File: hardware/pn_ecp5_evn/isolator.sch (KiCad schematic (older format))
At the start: 12 parts, among them U901 ADS7868, U902 ADS7868, U903 Si8640BB-B-IU, U904 Si8640BB-B-IU, U905 Si8642BB-B-IU

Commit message: first pass footprint assignment on pn r0
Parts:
- C901, C902: value C_Small -> 1 uF; footprint (none) -> Capacitor_SMD:C_0402_1005Metric
- C903, C904, C906, C907: value C_Small -> 100 nF; footprint (none) -> Capacitor_SMD:C_0402_1005Metric
- C905: value C_Small -> DNI; footprint (none) -> Capacitor_SMD:C_0402_1005Metric
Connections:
- net BUF_~PD: now reaches U905.11 (B4)
- net BUF_~PD~_ISO: now reaches U905.6 (A4)
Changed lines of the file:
@@
 P 2500 3950
 F 0 "C902" H 2592 3996 50  0000 L CNN
-F 1 "C_Small" H 2592 3905 50  0000 L CNN
-F 2 "" H 2500 3950 50  0001 C CNN
+F 1 "1 uF" H 2592 3905 50  0000 L CNN
+F 2 "Capacitor_SMD:C_0402_1005Metric" H 2500 3950 50  0001 C CNN
 F 3 "~" H 2500 3950 50  0001 C CNN
 	1    2500 3950
@@
 P 2500 2150
 F 0 "C901" H 2592 2196 50  0000 L CNN
-F 1 "C_Small" H 2592 2105 50  0000 L CNN
-F 2 "" H 2500 2150 50  0001 C CNN
+F 1 "1 uF" H 2592 2105 50  0000 L CNN
+F 2 "Capacitor_SMD:C_0402_1005Metric" H 2500 2150 50  0001 C CNN
 F 3 "~" H 2500 2150 50  0001 C CNN
 	1    2500 2150
@@
 P 5500 5850
 F 0 "C905" V 5271 5850 50  0000 C CNN
-F 1 "C_Small" V 5362 5850 50  0000 C CNN
-F 2 "" H 5500 5850 50  0001 C CNN
+F 1 "DNI" V 5362 5850 50  0000 C CNN
+F 2 "Capacitor_SMD:C_0402_1005Metric" H 5500 5850 50  0001 C CNN
 F 3 "~" H 5500 5850 50  0001 C CNN
 	1    5500 5850
@@
 P 7350 1850
 F 0 "C906" H 7442 1896 50  0000 L CNN
-F 1 "C_Small" H 7442 1805 50  0000 L CNN
-F 2 "" H 7350 1850 50  0001 C CNN
+F 1 "100 nF" H 7442 1805 50  0000 L CNN
+F 2 "Capacitor_SMD:C_0402_1005Metric" H 7350 1850 50  0001 C CNN
 F 3 "~" H 7350 1850 50  0001 C CNN
 	1    7350 1850
@@
 P 7900 1850
 F 0 "C907" H 7992 1896 50  0000 L CNN
-F 1 "C_Small" H 7992 1805 50  0000 L CNN
-F 2 "" H 7900 1850 50  0001 C CNN
+F 1 "100 nF" H 7992 1805 50  0000 L CNN
+F 2 "Capacitor_SMD:C_0402_1005Metric" H 7900 1850 50  0001 C CNN
 F 3 "~" H 7900 1850 50  0001 C CNN
 	1    7900 1850
@@
 P 3750 5900
 F 0 "C904" H 3842 5946 50  0000 L CNN
-F 1 "C_Small" H 3842 5855 50  0000 L CNN
-F 2 "" H 3750 5900 50  0001 C CNN
+F 1 "100 nF" H 3842 5855 50  0000 L CNN
+F 2 "Capacitor_SMD:C_0402_1005Metric" H 3750 5900 50  0001 C CNN
 F 3 "~" H 3750 5900 50  0001 C CNN
 	1    3750 5900
@@
 P 3150 5900
 F 0 "C903" H 3242 5946 50  0000 L CNN
-F 1 "C_Small" H 3242 5855 50  0000 L CNN
-F 2 "" H 3150 5900 50  0001 C CNN
+F 1 "100 nF" H 3242 5855 50  0000 L CNN
+F 2 "Capacitor_SMD:C_0402_1005Metric" H 3150 5900 50  0001 C CNN
 F 3 "~" H 3150 5900 50  0001 C CNN
 	1    3150 5900
@@
 Wire Wire Line
 	3150 5650 3150 5800
+Text HLabel 6400 5100 2    50   Input ~ 0
+BUF_~PD
+Wire Wire Line
+	6400 5100 5900 5100
+Text HLabel 4600 5100 0    50   Output ~ 0
+BUF_~PD~_ISO
+Wire Wire Line
+	4600 5100 5100 5100
 $EndSCHEMATC

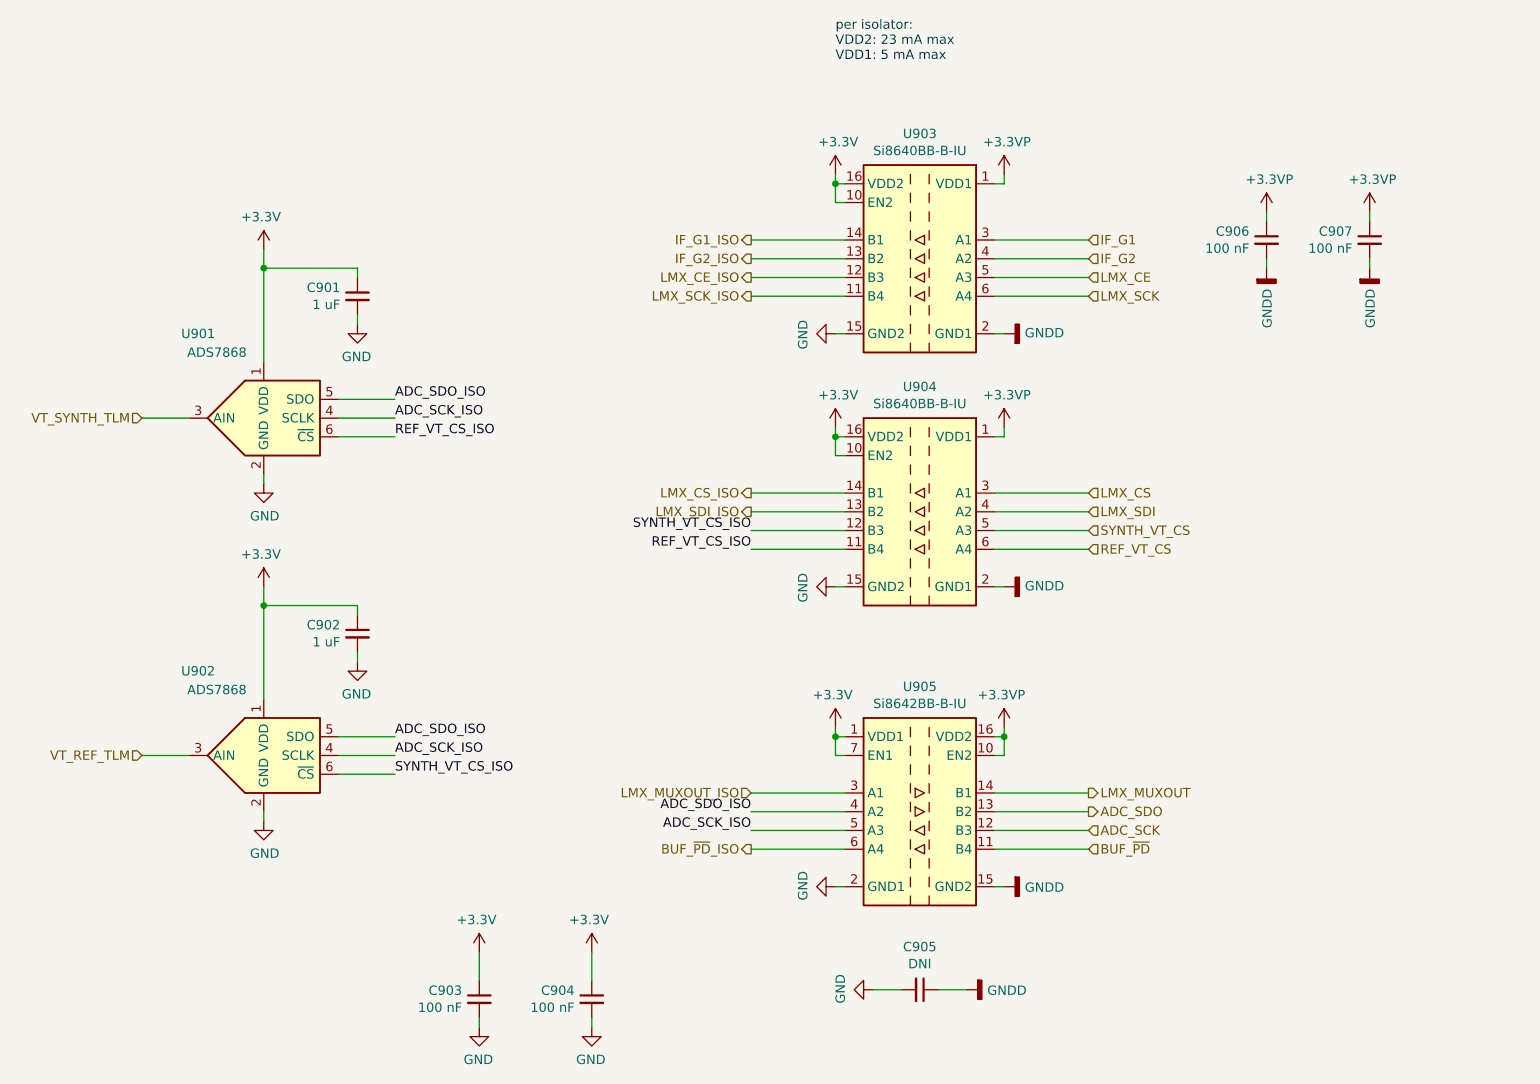
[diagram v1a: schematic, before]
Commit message: started component placement on phase noise analyzer
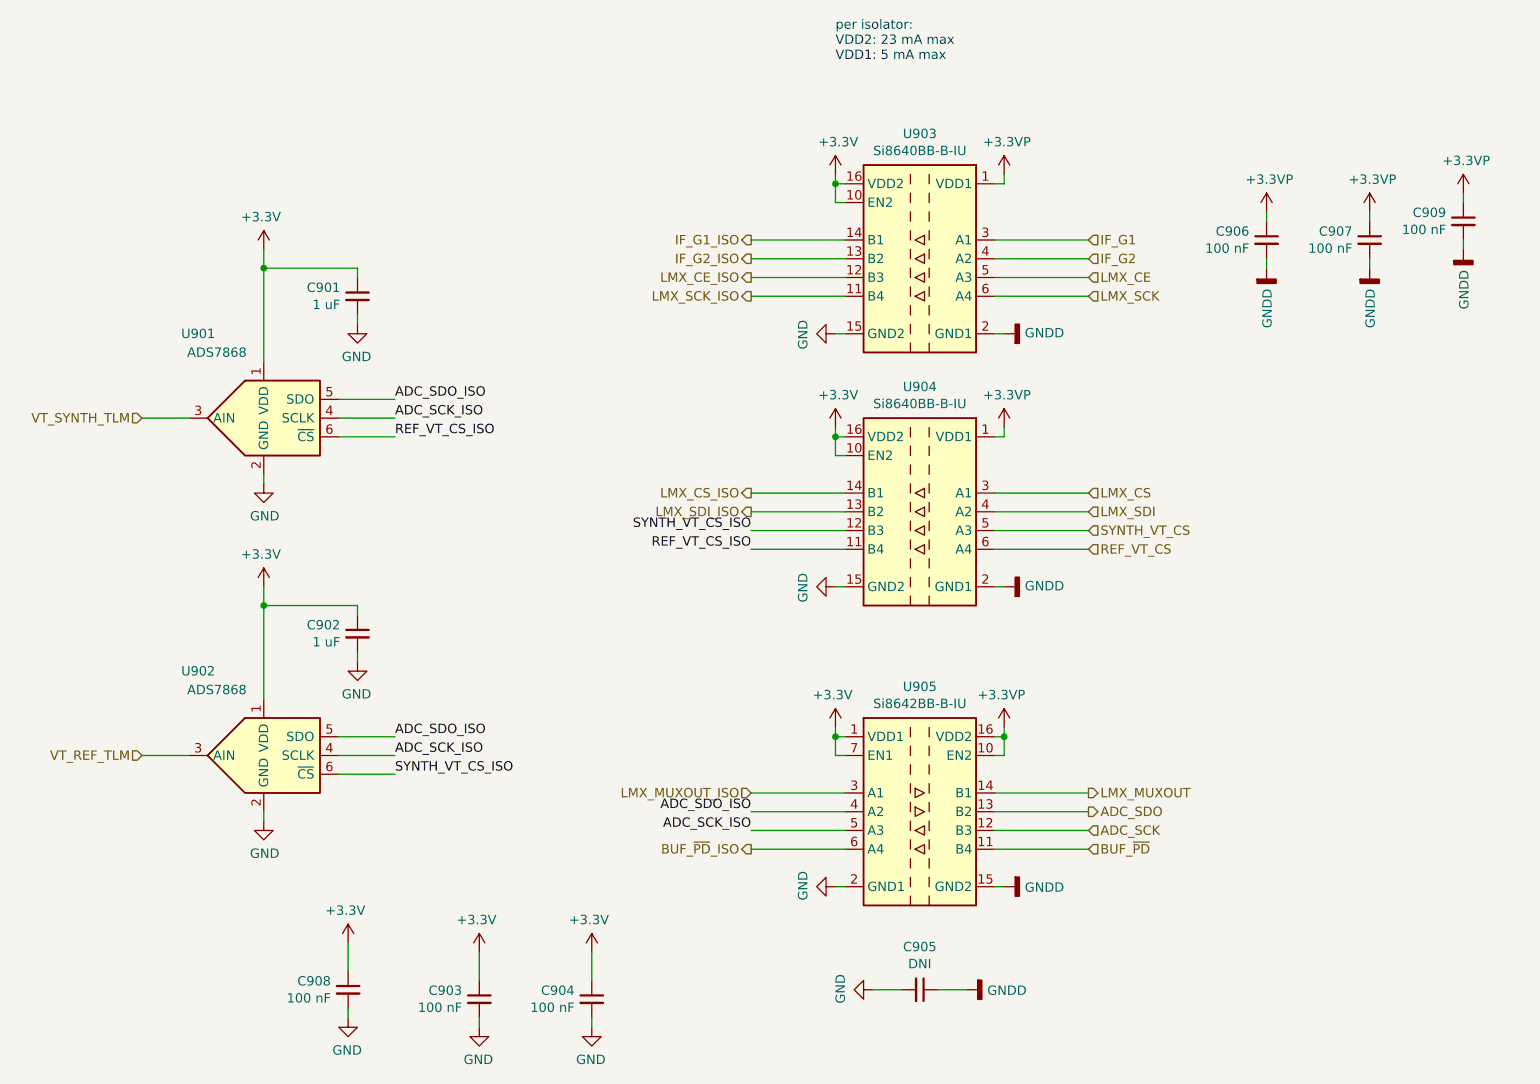
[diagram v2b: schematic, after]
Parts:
- added C908, C909: 100 nF, Capacitor_SMD:C_0402_1005Metric, symbol Device:C_Small
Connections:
- net +3.3VP: now also C909.1
- net +3V3: now also C908.1
- net GND: now also C908.2
- net GNDD: now also C909.2
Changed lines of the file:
@@
 Wire Wire Line
 	4600 5100 5100 5100
+Wire Wire Line
+	2450 5950 2450 6000
+$Comp
+L power:GND #PWR?
+U 1 1 5F3C236D
+P 2450 6000
+AR Path="/5F2678A0/5F3C236D" Ref="#PWR?"  Part="1"
+AR Path="/6047B31A/5F3C236D" Ref="#PWR0285"  Part="1"
+F 0 "#PWR0285" H 2450 5750 50  0001 C CNN
+F 1 "GND" H 2455 5827 50  0000 C CNN
+F 2 "" H 2450 6000 50  0001 C CNN
+F 3 "" H 2450 6000 50  0001 C CNN
+	1    2450 6000
+	-1   0    0    -1
+$EndComp
+$Comp
+L Device:C_Small C908
+U 1 1 5F3C2373
+P 2450 5850
+F 0 "C908" H 2542 5896 50  0000 L CNN
+F 1 "100 nF" H 2542 5805 50  0000 L CNN
+F 2 "Capacitor_SMD:C_0402_1005Metric" H 2450 5850 50  0001 C CNN
+F 3 "~" H 2450 5850 50  0001 C CNN
+	1    2450 5850
+	-1   0    0    -1
+$EndComp
+$Comp
+L power:+3.3V #PWR?
+U 1 1 5F3C2379
+P 2450 5600
+AR Path="/5F2678A0/5F3C2379" Ref="#PWR?"  Part="1"
+AR Path="/6047B31A/5F3C2379" Ref="#PWR0286"  Part="1"
+F 0 "#PWR0286" H 2450 5450 50  0001 C CNN
+F 1 "+3.3V" H 2465 5773 50  0000 C CNN
+F 2 "" H 2450 5600 50  0001 C CNN
+F 3 "" H 2450 5600 50  0001 C CNN
+	1    2450 5600
+	-1   0    0    -1
+$EndComp
+Wire Wire Line
+	2450 5600 2450 5750
+$Comp
+L power:+3.3VP #PWR?
+U 1 1 5F3C72BF
+P 8400 1600
+AR Path="/5F3C72BF" Ref="#PWR?"  Part="1"
+AR Path="/6047B31A/5F3C72BF" Ref="#PWR0287"  Part="1"
+F 0 "#PWR0287" H 8550 1550 50  0001 C CNN
+F 1 "+3.3VP" H 8415 1773 50  0000 C CNN
+F 2 "" H 8400 1600 50  0001 C CNN
+F 3 "" H 8400 1600 50  0001 C CNN
+	1    8400 1600
+	1    0    0    -1
+$EndComp
+$Comp
+L Device:C_Small C909
+U 1 1 5F3C72C5
+P 8400 1750
+F 0 "C909" H 8492 1796 50  0000 L CNN
+F 1 "100 nF" H 8492 1705 50  0000 L CNN
+F 2 "Capacitor_SMD:C_0402_1005Metric" H 8400 1750 50  0001 C CNN
+F 3 "~" H 8400 1750 50  0001 C CNN
+	1    8400 1750
+	-1   0    0    -1
+$EndComp
+$Comp
+L power:GNDD #PWR?
+U 1 1 5F3C72CB
+P 8400 1900
+AR Path="/5F3C72CB" Ref="#PWR?"  Part="1"
+AR Path="/6047B31A/5F3C72CB" Ref="#PWR0288"  Part="1"
+F 0 "#PWR0288" H 8400 1650 50  0001 C CNN
+F 1 "GNDD" V 8404 1790 50  0000 R CNN
+F 2 "" H 8400 1900 50  0001 C CNN
+F 3 "" H 8400 1900 50  0001 C CNN
+	1    8400 1900
+	1    0    0    -1
+$EndComp
+Wire Wire Line
+	8400 1900 8400 1850
+Wire Wire Line
+	8400 1650 8400 1600
 $EndSCHEMATC

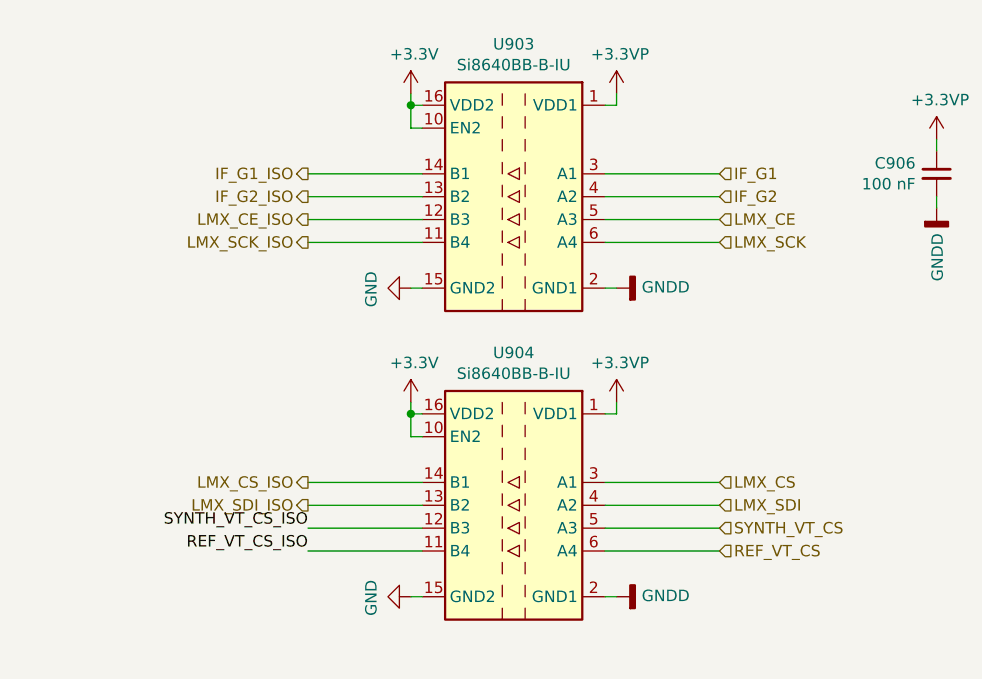
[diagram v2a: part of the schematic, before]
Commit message: work on routing phase noise downconverter
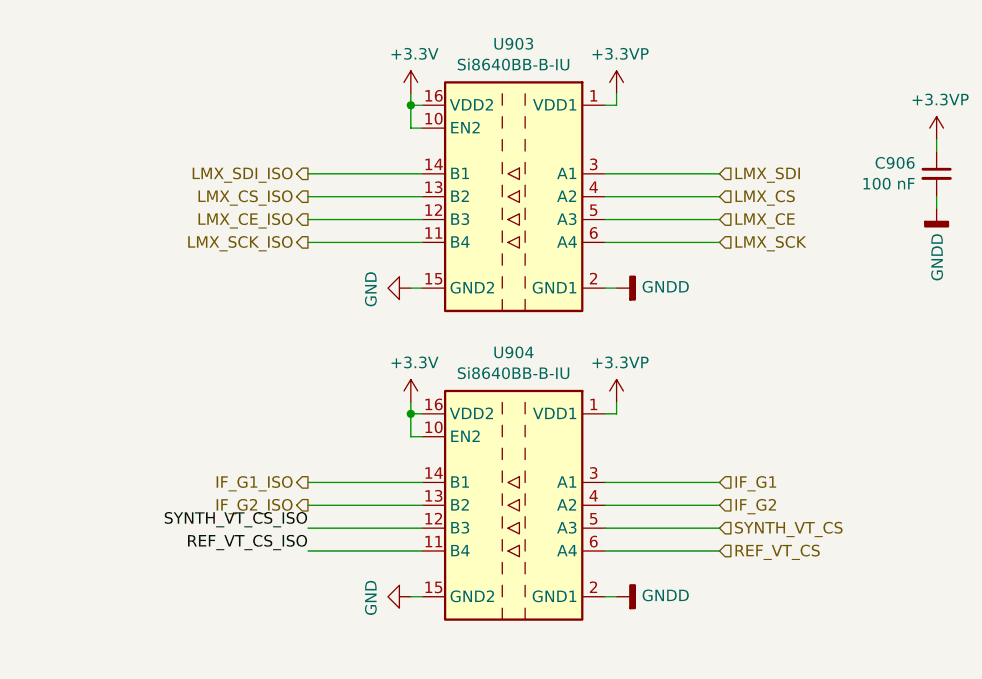
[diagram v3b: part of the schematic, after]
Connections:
- net IF_G1: now also U904.3 (A1); no longer U903.3 (A1)
- net IF_G1_ISO: now also U904.14 (B1); no longer U903.14 (B1)
- net IF_G2: now also U904.4 (A2); no longer U903.4 (A2)
- net IF_G2_ISO: now also U904.13 (B2); no longer U903.13 (B2)
- net LMX_CS: now also U903.4 (A2); no longer U904.3 (A1)
- net LMX_CS_ISO: now also U903.13 (B2); no longer U904.14 (B1)
- net LMX_SDI: now also U903.3 (A1); no longer U904.4 (A2)
- net LMX_SDI_ISO: now also U903.14 (B1); no longer U904.13 (B2)
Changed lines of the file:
@@
 	5900 2050 6400 2050
 Wire Wire Line
-	5900 1950 6400 1950
+	5900 3300 6400 3300
 Wire Wire Line
-	5900 1850 6400 1850
+	5900 3200 6400 3200
 Wire Wire Line
 	4600 2050 5100 2050
 Wire Wire Line
-	4600 1950 5100 1950
+	4600 3300 5100 3300
 Wire Wire Line
-	4600 1850 5100 1850
+	4600 3200 5100 3200
 $Comp
 L Isolator:Si8640BB-B-IU U904
@@
 	5900 3400 6400 3400
 Wire Wire Line
-	5900 3300 6400 3300
+	5900 1850 6400 1850
 Wire Wire Line
-	5900 3200 6400 3200
+	5900 1950 6400 1950
 Wire Wire Line
 	4600 3500 5100 3500
@@
 	4600 3400 5100 3400
 Wire Wire Line
-	4600 3300 5100 3300
+	4600 1850 5100 1850
 Wire Wire Line
-	4600 3200 5100 3200
-Text HLabel 4600 1850 0    50   Output ~ 0
+	4600 1950 5100 1950
+Text HLabel 4600 3200 0    50   Output ~ 0
 IF_G1_ISO
-Text HLabel 4600 1950 0    50   Output ~ 0
+Text HLabel 4600 3300 0    50   Output ~ 0
 IF_G2_ISO
 Text HLabel 4600 2050 0    50   Output ~ 0
@@
 Text HLabel 4600 2150 0    50   Output ~ 0
 LMX_SCK_ISO
-Text HLabel 4600 3200 0    50   Output ~ 0
+Text HLabel 4600 1950 0    50   Output ~ 0
 LMX_CS_ISO
-Text HLabel 4600 3300 0    50   Output ~ 0
+Text HLabel 4600 1850 0    50   Output ~ 0
 LMX_SDI_ISO
-Text HLabel 6400 1850 2    50   Input ~ 0
+Text HLabel 6400 3200 2    50   Input ~ 0
 IF_G1
-Text HLabel 6400 1950 2    50   Input ~ 0
+Text HLabel 6400 3300 2    50   Input ~ 0
 IF_G2
 Text HLabel 6400 2050 2    50   Input ~ 0
@@
 Text HLabel 6400 2150 2    50   Input ~ 0
 LMX_SCK
-Text HLabel 6400 3200 2    50   Input ~ 0
+Text HLabel 6400 1950 2    50   Input ~ 0
 LMX_CS
-Text HLabel 6400 3300 2    50   Input ~ 0
+Text HLabel 6400 1850 2    50   Input ~ 0
 LMX_SDI
 Text HLabel 6400 3400 2    50   Input ~ 0
